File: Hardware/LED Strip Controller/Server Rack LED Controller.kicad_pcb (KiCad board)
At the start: 2 copper layers, 26 parts, among them Q1 IRF540N, Q10 IRF540N, Q11 IRF540N, Q12 IRF540N, Q13 IRF540N, Q2 IRF540N, Q3 Q_PMOS_SDG, Q4 IRF540N, Q5 IRF540N, Q6 IRF540N, Q7 IRF540N, Q8 IRF540N, Q9 IRF540N, U1 STM32F103C8Tx, U2 LM2596S-5, U3 LD1117S50TR_SOT223

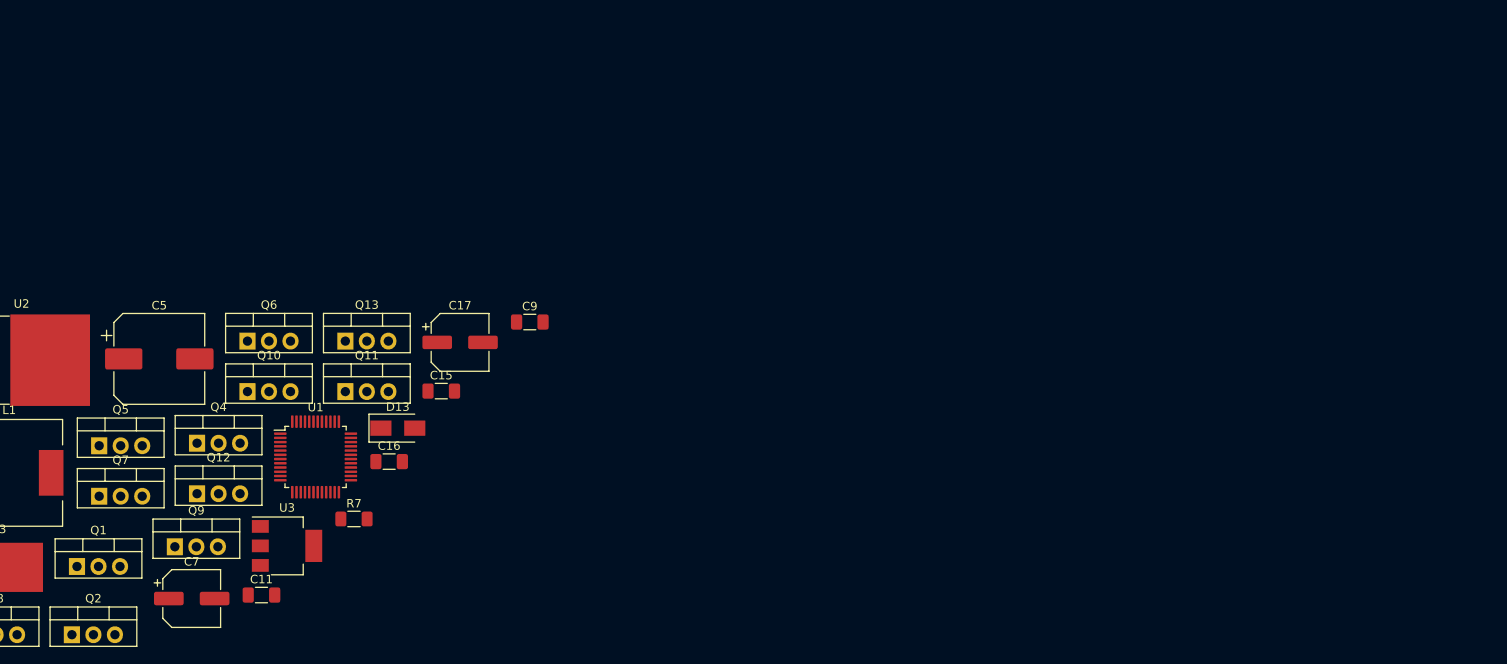
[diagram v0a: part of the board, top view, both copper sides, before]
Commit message: Adding updated PCB Schematic, still to add USB C connector and JLCPCB Part Numbers and values
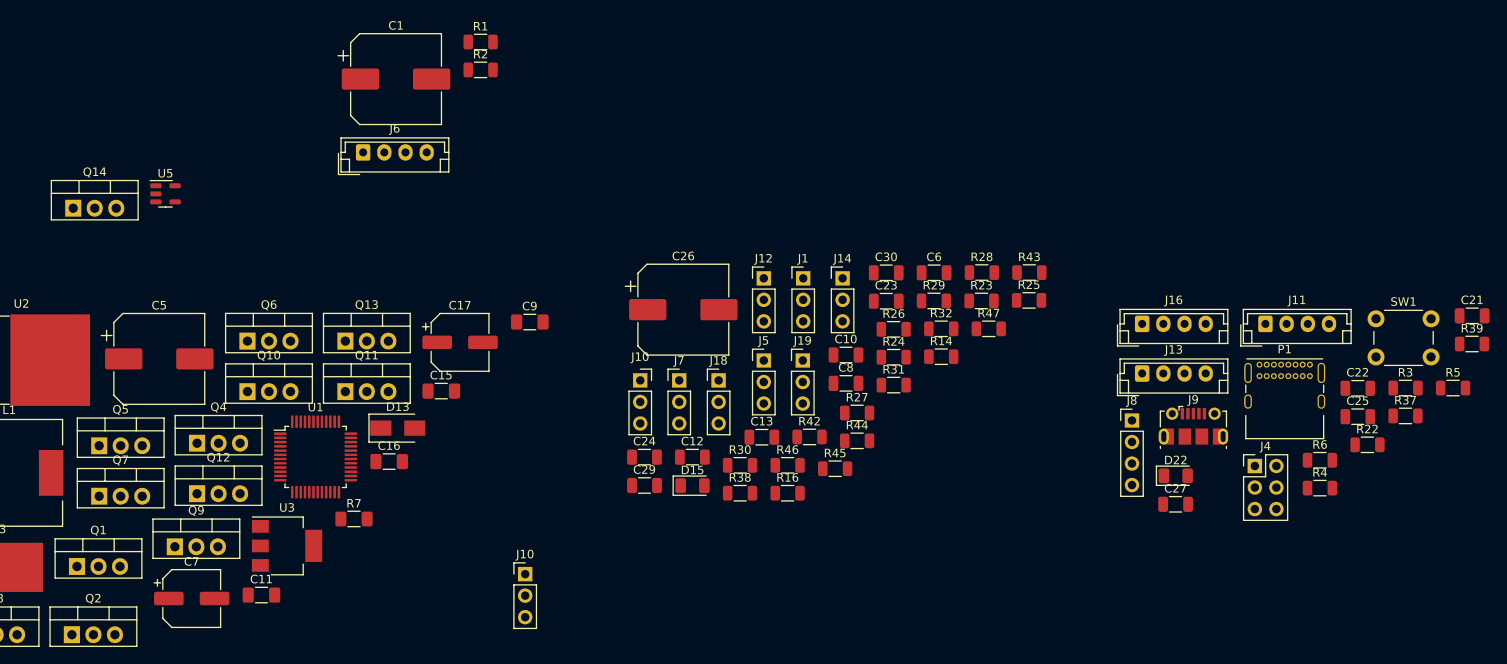
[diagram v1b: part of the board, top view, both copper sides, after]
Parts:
- added C1: C_Polarized, Capacitor_SMD:CP_Elec_10x10.5, F.Cu at (127.0, 27.9)
- added C10: 100nF, Capacitor_SMD:C_1206_3216Metric, F.Cu at (180.1, 60.5)
- added C12: 100nF, Capacitor_SMD:C_1206_3216Metric, F.Cu at (162.0, 72.5)
- added C13: 100nF, Capacitor_SMD:C_1206_3216Metric, F.Cu at (170.2, 70.2)
- added C21: 1uF, Capacitor_SMD:C_1206_3216Metric, F.Cu at (254.0, 55.9)
- added C22: 100nF, Capacitor_SMD:C_1206_3216Metric, F.Cu at (240.5, 64.4)
- added C23: 100nF, Capacitor_SMD:C_1206_3216Metric, F.Cu at (184.8, 54.1)
- added C24: 10nF, Capacitor_SMD:C_1206_3216Metric, F.Cu at (156.3, 72.5)
- added C25: 1uF, Capacitor_SMD:C_1206_3216Metric, F.Cu at (240.5, 67.8)
- added C26: C_Polarized, Capacitor_SMD:CP_Elec_10x10.5, F.Cu at (160.9, 55.1)
- added C27: 100nF, Capacitor_SMD:C_1206_3216Metric, F.Cu at (219.0, 78.1)
- added C29: 01.uF, Capacitor_SMD:C_1206_3216Metric, F.Cu at (156.3, 75.9)
- added C30: 1uF, Capacitor_SMD:C_1206_3216Metric, F.Cu at (184.8, 50.8)
- added C6: 100nF, Capacitor_SMD:C_1206_3216Metric, F.Cu at (190.5, 50.8)
- added C8: 100nF, Capacitor_SMD:C_1206_3216Metric, F.Cu at (180.1, 63.9)
- added D15: LED, LED_SMD:LED_1206_3216Metric, F.Cu at (162.0, 75.9)
- added D22: LED, LED_SMD:LED_1206_3216Metric, F.Cu at (219.0, 74.8)
- added J1: Conn_01x03_Male, Connector_PinHeader_2.54mm:PinHeader_1x03_P2.54mm_Vertical, F.Cu at (175.1, 51.5)
- added J10: Conn_01x03_Female, Connector_PinSocket_2.54mm:PinSocket_1x03_P2.54mm_Vertical, F.Cu at (155.8, 63.5)
- added J10: UART, Connector_PinHeader_2.54mm:PinHeader_1x03_P2.54mm_Vertical, F.Cu at (142.2, 86.4)
- added J11: CONN_2, Connector_JST:JST_EH_B4B-EH-A_1x04_P2.50mm_Vertical, F.Cu at (229.6, 56.8)
- added J12: Conn_01x03_Male, Connector_PinHeader_2.54mm:PinHeader_1x03_P2.54mm_Vertical, F.Cu at (170.4, 51.5)
- added J13: CONN_3, Connector_JST:JST_EH_B4B-EH-A_1x04_P2.50mm_Vertical, F.Cu at (215.1, 62.7)
- added J14: Conn_01x03_Male, Connector_PinHeader_2.54mm:PinHeader_1x03_P2.54mm_Vertical, F.Cu at (179.7, 51.5)
- added J16: CONN_4, Connector_JST:JST_EH_B4B-EH-A_1x04_P2.50mm_Vertical, F.Cu at (215.1, 56.8)
- added J18: Conn_01x03_Male, Connector_PinHeader_2.54mm:PinHeader_1x03_P2.54mm_Vertical, F.Cu at (165.1, 63.5)
- added J19: Conn_01x03_Male, Connector_PinHeader_2.54mm:PinHeader_1x03_P2.54mm_Vertical, F.Cu at (175.0, 61.1)
- added J4: Conn_02x03_Odd_Even, Connector_PinHeader_2.54mm:PinHeader_2x03_P2.54mm_Vertical, F.Cu at (228.3, 73.6)
- added J5: Conn_01x03_Female, Connector_PinHeader_2.54mm:PinHeader_1x03_P2.54mm_Vertical, F.Cu at (170.4, 61.1)
- added J6: CONN_1, Connector_JST:JST_EH_B4B-EH-A_1x04_P2.50mm_Vertical, F.Cu at (123.1, 36.6)
- added J7: Conn_01x03_Male, Connector_PinHeader_2.54mm:PinHeader_1x03_P2.54mm_Vertical, F.Cu at (160.4, 63.5)
- added J8: SWD, Connector_PinHeader_2.54mm:PinHeader_1x04_P2.54mm_Vertical, F.Cu at (213.8, 68.2)
- added J9: USB_B_Micro, Connector_USB:USB_Micro-B_Molex-105017-0001, F.Cu at (221.1, 68.9)
- added P1: USB_C_Plug, Connector_USB:USB_C_Receptacle_GCT_USB4085, F.Cu at (228.9, 61.6)
- added Q14: IRF540N, Package_TO_SOT_THT:TO-220-3_Vertical, F.Cu at (88.9, 43.2)
- added R1: 10k, Resistor_SMD:R_1206_3216Metric, F.Cu at (137.0, 23.6)
- added R14: 10K, Resistor_SMD:R_1206_3216Metric, F.Cu at (191.3, 60.7)
- added R16: R, Resistor_SMD:R_1206_3216Metric, F.Cu at (173.2, 76.8)
- added R2: 100k, Resistor_SMD:R_1206_3216Metric, F.Cu at (137.0, 26.9)
- added R22: R, Resistor_SMD:R_1206_3216Metric, F.Cu at (241.6, 71.1)
- added R23: R, Resistor_SMD:R_1206_3216Metric, F.Cu at (196.1, 54.1)
- added R24: R, Resistor_SMD:R_1206_3216Metric, F.Cu at (185.7, 60.8)
- added R25: R, Resistor_SMD:R_1206_3216Metric, F.Cu at (201.7, 54.1)
- added R26: R, Resistor_SMD:R_1206_3216Metric, F.Cu at (185.7, 57.5)
- added R27: R, Resistor_SMD:R_1206_3216Metric, F.Cu at (181.4, 67.3)
- added R28: R, Resistor_SMD:R_1206_3216Metric, F.Cu at (196.1, 50.8)
- added R29: 10K, Resistor_SMD:R_1206_3216Metric, F.Cu at (190.5, 54.1)
- added R3: R, Resistor_SMD:R_1206_3216Metric, F.Cu at (246.1, 64.4)
- added R30: 10K, Resistor_SMD:R_1206_3216Metric, F.Cu at (167.6, 73.5)
- added R31: 10K, Resistor_SMD:R_1206_3216Metric, F.Cu at (185.7, 64.0)
- added R32: 10K, Resistor_SMD:R_1206_3216Metric, F.Cu at (191.3, 57.4)
- added R37: 100K, Resistor_SMD:R_1206_3216Metric, F.Cu at (246.1, 67.7)
- added R38: R, Resistor_SMD:R_1206_3216Metric, F.Cu at (167.6, 76.8)
- added R39: 100K, Resistor_SMD:R_1206_3216Metric, F.Cu at (254.0, 59.2)
- added R4: R, Resistor_SMD:R_1206_3216Metric, F.Cu at (236.0, 76.2)
- added R42: 20R, Resistor_SMD:R_1206_3216Metric, F.Cu at (175.8, 70.2)
- added R43: 20R, Resistor_SMD:R_1206_3216Metric, F.Cu at (201.7, 50.8)
- added R44: 4.7K, Resistor_SMD:R_1206_3216Metric, F.Cu at (181.4, 70.6)
- added R45: 1M, Resistor_SMD:R_1206_3216Metric, F.Cu at (178.8, 73.9)
- added R46: 20R, Resistor_SMD:R_1206_3216Metric, F.Cu at (173.2, 73.5)
- added R47: 20R, Resistor_SMD:R_1206_3216Metric, F.Cu at (196.9, 57.4)
- added R5: R, Resistor_SMD:R_1206_3216Metric, F.Cu at (251.7, 64.4)
- added R6: R, Resistor_SMD:R_1206_3216Metric, F.Cu at (236.0, 72.9)
- added SW1: SW_Push_Dual, Button_Switch_THT:SW_PUSH_6mm, F.Cu at (242.7, 56.2)
- added U5: INA169, Package_TO_SOT_SMD:SOT-23-5, F.Cu at (99.8, 41.5)
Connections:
- C11 pad 2: GND -> CURR_SENSE
- C15 pad 2: GND -> CURR_SENSE
- C16 pad 2: GND -> CURR_SENSE
- C17 pad 2: GND -> CURR_SENSE
- C5 pad 2: GND -> CURR_SENSE
- C7 pad 2: GND -> CURR_SENSE
- C9 pad 2: GND -> CURR_SENSE
- D13 pad 2: GND -> CURR_SENSE
- Q1 pad 3: GND -> CURR_SENSE
- Q10 pad 3: GND -> CURR_SENSE
- Q11 pad 3: GND -> CURR_SENSE
- Q12 pad 3: GND -> CURR_SENSE
- Q13 pad 3: GND -> CURR_SENSE
- Q2 pad 3: GND -> CURR_SENSE
- Q4 pad 3: GND -> CURR_SENSE
- Q5 pad 3: GND -> CURR_SENSE
- Q6 pad 3: GND -> CURR_SENSE
- Q7 pad 3: GND -> CURR_SENSE
- Q8 pad 3: GND -> CURR_SENSE
- Q9 pad 3: GND -> CURR_SENSE
- R7 pad 2: GND -> CURR_SENSE
- U1 pad 10: PWM_4_GREEN -> PWM_1_GREEN
- U1 pad 11: PWM_2_BLUE -> PWM_1_RED
- U1 pad 12: PWM_2_RED -> PWM_1_BLUE
- U1 pad 13: PWM_2_GREEN -> PWM_4_GREEN
- U1 pad 14: unconnected-(U1-Pad14) -> CURR_SENSE
- U1 pad 15: unconnected-(U1-Pad15) -> VS_SENSE
- U1 pad 16: PWM_4_RED -> PWM_2_GREEN
- U1 pad 17: PWM_1_BLUE -> PWM_2_BLUE
- U1 pad 18: PWM_1_RED -> PWM_2_BLUE
- U1 pad 19: PWM_1_GREEN -> PWM_4_RED
- U1 pad 23: unconnected-(U1-Pad23) -> CURR_SENSE
- U1 pad 24: unconnected-(U1-Pad24) -> VDDA
- U1 pad 3: Net-(C2-Pad1) -> OSC32_IN
- U1 pad 32: Net-(J9-Pad2) -> STM32_USB-
- U1 pad 33: Net-(J9-Pad3) -> STM32_USB+
- U1 pad 35: unconnected-(U1-Pad35) -> CURR_SENSE
- U1 pad 36: unconnected-(U1-Pad36) -> VDDA
- U1 pad 38: unconnected-(U1-Pad38) -> FAN_SIG
- U1 pad 4: Net-(C3-Pad1) -> OSC32_OUT
- U1 pad 47: unconnected-(U1-Pad47) -> CURR_SENSE
- U1 pad 48: unconnected-(U1-Pad48) -> VDDA
- U1 pad 5: unconnected-(U1-Pad5) -> OSC_IN
- U1 pad 6: unconnected-(U1-Pad6) -> OSC_OUT
- U1 pad 7: unconnected-(U1-Pad7) -> RESET
- U1 pad 8: unconnected-(U1-Pad8) -> CURR_SENSE
- U1 pad 9: unconnected-(U1-Pad9) -> VDDA
- U2 pad 3: GND -> CURR_SENSE
- U2 pad 5: GND -> CURR_SENSE
- U3 pad 1: GND -> CURR_SENSE

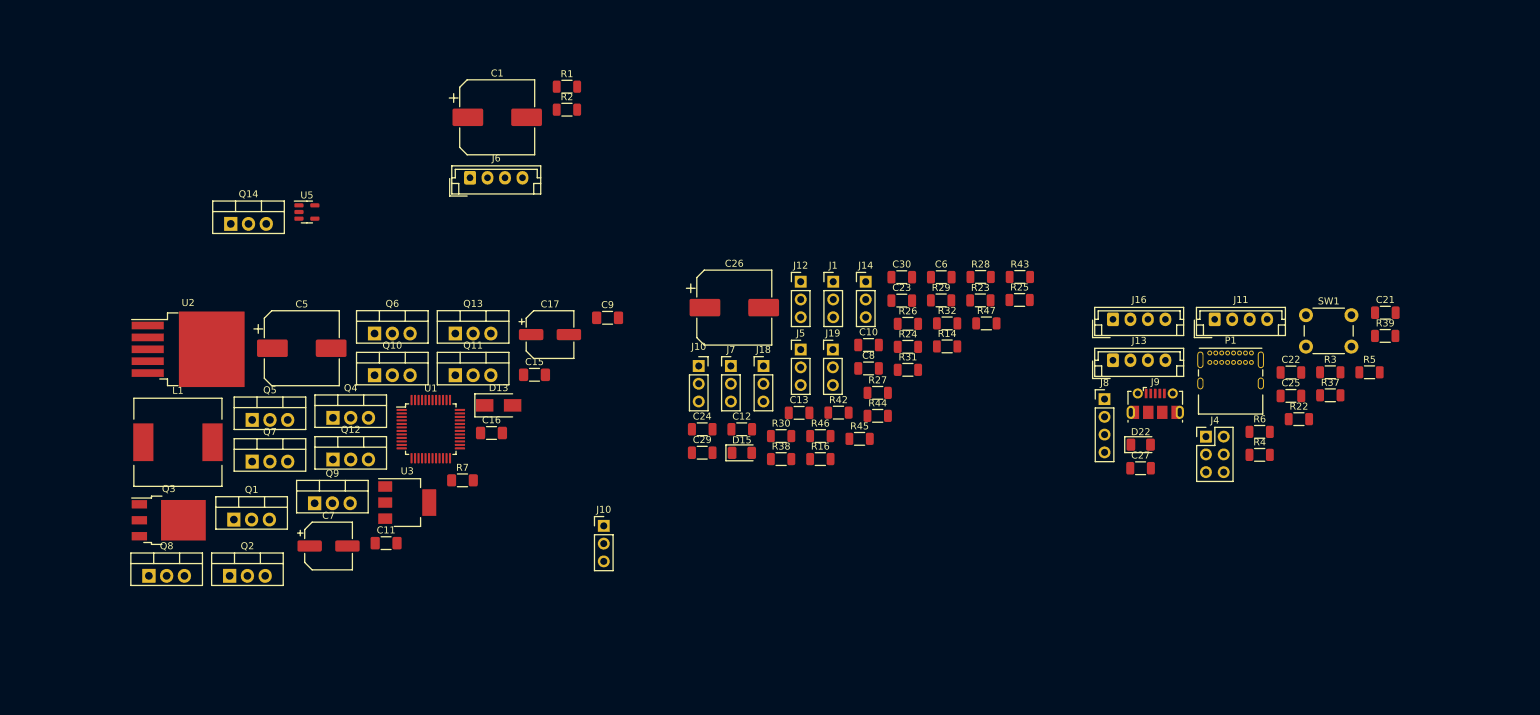
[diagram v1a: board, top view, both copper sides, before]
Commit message: Adding updated PCB Schematic, need to source JLCPCB SMT Parts and do layout
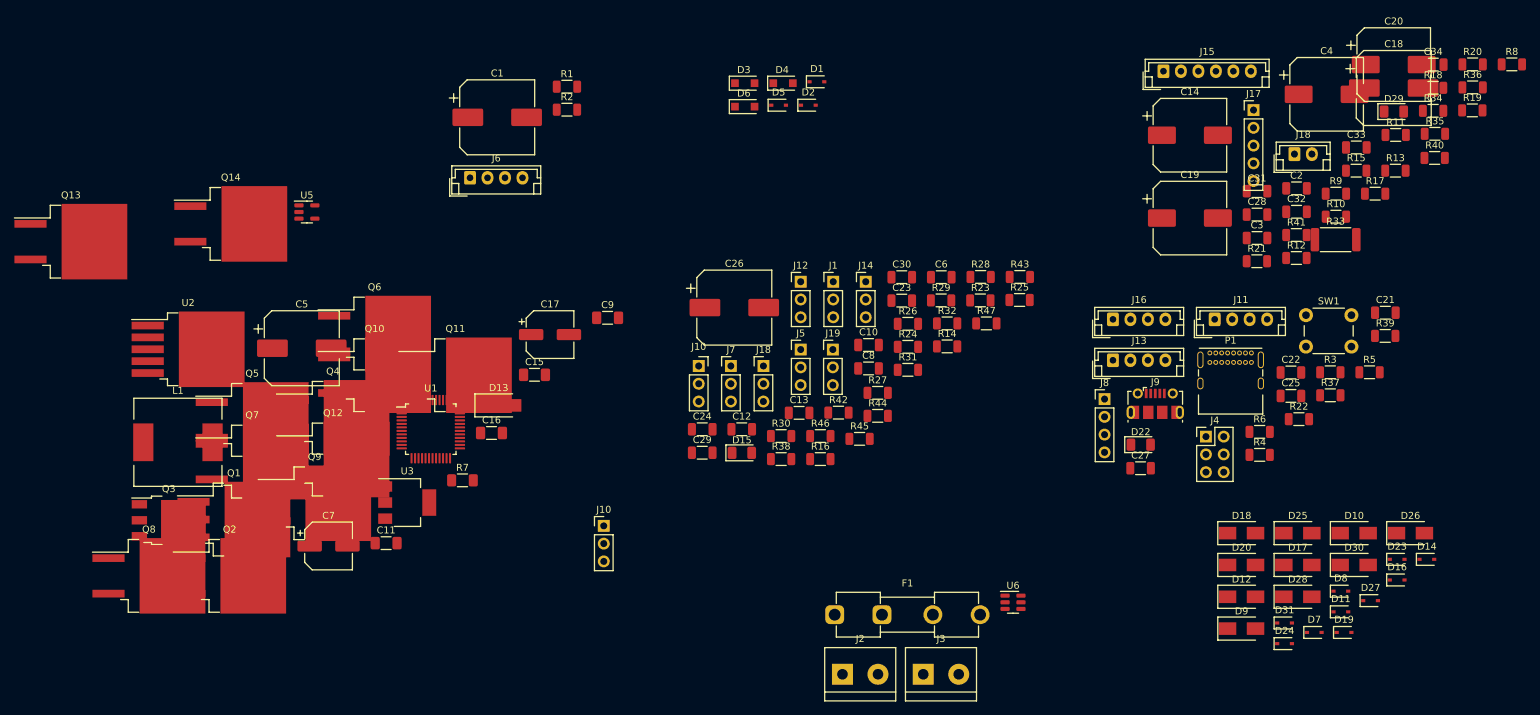
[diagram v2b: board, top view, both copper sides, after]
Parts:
- added C14: 100uF, Capacitor_SMD:CP_Elec_10x10, F.Cu at (226.1, 30.5)
- added C18: 10uF, Capacitor_SMD:CP_Elec_10x10.5, F.Cu at (255.2, 23.8)
- added C19: 100uF, Capacitor_SMD:CP_Elec_10x10, F.Cu at (226.1, 42.4)
- added C2: C, Capacitor_SMD:C_1206_3216Metric, F.Cu at (241.3, 38.1)
- added C20: 10uF, Capacitor_SMD:CP_Elec_10x10, F.Cu at (255.2, 20.4)
- added C28: 01.uF, Capacitor_SMD:C_1206_3216Metric, F.Cu at (235.7, 41.9)
- added C3: C, Capacitor_SMD:C_1206_3216Metric, F.Cu at (235.7, 45.2)
- added C31: C, Capacitor_SMD:C_1206_3216Metric, F.Cu at (235.7, 38.5)
- added C32: C, Capacitor_SMD:C_1206_3216Metric, F.Cu at (241.3, 41.5)
- added C33: 1u, Capacitor_SMD:C_1206_3216Metric, F.Cu at (249.8, 32.2)
- added C34: 10n, Capacitor_SMD:C_1206_3216Metric, F.Cu at (260.9, 20.4)
- added C4: 100uF, Capacitor_SMD:CP_Elec_10x10, F.Cu at (245.6, 24.6)
- added D1: 1N4148, Diode_SMD:D_SOD-323, F.Cu at (172.7, 22.9)
- added D10: 1N4001, Diode_SMD:D_SMA, F.Cu at (249.5, 87.4)
- added D11: 1N4148, Diode_SMD:D_SOD-323, F.Cu at (247.6, 98.7)
- added D12: 1N4001, Diode_SMD:D_SMA, F.Cu at (233.4, 96.5)
- added D14: 1N4148, Diode_SMD:D_SOD-323, F.Cu at (259.9, 91.2)
- added D16: 1N4148, Diode_SMD:D_SOD-323, F.Cu at (255.7, 94.1)
- added D17: 1N4001, Diode_SMD:D_SMA, F.Cu at (241.5, 92.0)
- added D18: 1N4001, Diode_SMD:D_SMA, F.Cu at (233.4, 87.4)
- added D19: 1N4148, Diode_SMD:D_SOD-323, F.Cu at (248.1, 101.6)
- added D2: 1N4148, Diode_SMD:D_SOD-323, F.Cu at (171.5, 26.2)
- added D20: 1N4001, Diode_SMD:D_SMA, F.Cu at (233.4, 92.0)
- added D23: 1N4148, Diode_SMD:D_SOD-323, F.Cu at (255.7, 91.2)
- added D24: 1N4148, Diode_SMD:D_SOD-323, F.Cu at (239.6, 103.2)
- added D25: 1N4001, Diode_SMD:D_SMA, F.Cu at (241.5, 87.4)
- added D26: 1N4001, Diode_SMD:D_SMA, F.Cu at (257.6, 87.4)
- added D27: 1N4148, Diode_SMD:D_SOD-323, F.Cu at (251.9, 97.0)
- added D28: 1N4001, Diode_SMD:D_SMA, F.Cu at (241.5, 96.5)
- added D29: RED LED, LED_SMD:LED_1206_3216Metric, F.Cu at (255.2, 27.1)
- added D3: 1N4001, Diode_SMD:D_SOD-123F, F.Cu at (162.4, 23.1)
- added D30: 1N5001, Diode_SMD:D_SMA, F.Cu at (249.5, 92.0)
- added D31: 1N4148, Diode_SMD:D_SOD-323, F.Cu at (239.6, 100.2)
- added D4: 1N4001, Diode_SMD:D_SOD-123F, F.Cu at (167.9, 23.1)
- added D5: 1N4148, Diode_SMD:D_SOD-323, F.Cu at (167.2, 26.2)
- added D6: 1N4001, Diode_SMD:D_SOD-123F, F.Cu at (162.4, 26.4)
- added D7: 1N4148, Diode_SMD:D_SOD-323, F.Cu at (243.8, 101.6)
- added D8: 1N4148, Diode_SMD:D_SOD-323, F.Cu at (247.6, 95.7)
- added D9: 1N4001, Diode_SMD:D_SMA, F.Cu at (233.4, 101.0)
- added F1: 1A, Fuse:Fuseholder_Clip-5x20mm_Eaton_1A5601-01_Inline_P20.80x6.76mm_D1.70mm_Horizontal, F.Cu at (175.3, 99.1)
- added J15: Conn_01x06_Female, Connector_JST:JST_EH_B6B-EH-A_1x06_P2.50mm_Vertical, F.Cu at (222.3, 21.4)
- added J17: TST, Connector_PinHeader_2.54mm:PinHeader_1x05_P2.54mm_Vertical, F.Cu at (235.2, 26.9)
- added J18: Conn_01x02_Female, Connector_JST:JST_EH_B2B-EH-A_1x02_P2.50mm_Vertical, F.Cu at (241.0, 33.2)
- added J2: Screw_Terminal_01x02, TerminalBlock:TerminalBlock_bornier-2_P5.08mm, F.Cu at (176.4, 107.6)
- added J3: PWR_SWITCH, TerminalBlock:TerminalBlock_bornier-2_P5.08mm, F.Cu at (187.9, 107.6)
- added R10: 10K, Resistor_SMD:R_1206_3216Metric, F.Cu at (246.9, 42.1)
- added R11: 10K, Resistor_SMD:R_1206_3216Metric, F.Cu at (255.5, 30.5)
- added R12: 100K, Resistor_SMD:R_1206_3216Metric, F.Cu at (241.3, 48.1)
- added R13: 100K, Resistor_SMD:R_1206_3216Metric, F.Cu at (255.4, 35.6)
- added R15: 10K, Resistor_SMD:R_1206_3216Metric, F.Cu at (249.8, 35.6)
- added R17: 100K, Resistor_SMD:R_1206_3216Metric, F.Cu at (252.5, 38.9)
- added R18: 10K, Resistor_SMD:R_1206_3216Metric, F.Cu at (260.8, 23.7)
- added R19: 10K, Resistor_SMD:R_1206_3216Metric, F.Cu at (266.4, 26.9)
- added R20: 100K, Resistor_SMD:R_1206_3216Metric, F.Cu at (266.5, 20.4)
- added R21: 100K, Resistor_SMD:R_1206_3216Metric, F.Cu at (235.6, 48.5)
- added R33: 0.1R, Resistor_SMD:R_2512_6332Metric, F.Cu at (246.9, 45.4)
- added R34: 10K, Resistor_SMD:R_1206_3216Metric, F.Cu at (260.8, 27.0)
- added R35: 1M, Resistor_SMD:R_1206_3216Metric, F.Cu at (261.1, 30.3)
- added R36: 10M, Resistor_SMD:R_1206_3216Metric, F.Cu at (266.5, 23.7)
- added R40: 10K, Resistor_SMD:R_1206_3216Metric, F.Cu at (261.1, 33.8)
- added R41: 100K, Resistor_SMD:R_1206_3216Metric, F.Cu at (241.3, 44.8)
- added R8: 10K, Resistor_SMD:R_1206_3216Metric, F.Cu at (272.1, 20.4)
- added R9: 100K, Resistor_SMD:R_1206_3216Metric, F.Cu at (246.9, 38.9)
- added U6: USBLC6-2SC6, Package_TO_SOT_SMD:SOT-23-6, F.Cu at (200.8, 97.3)
- C1, C26: value C_Polarized -> 100uF
- D15: value LED -> Green LED
- D22: value LED -> Blue LED
- Q1: value IRF540N -> IRF510N; footprint Package_TO_SOT_THT:TO-220-3_Vertical -> Package_TO_SOT_SMD:TO-263-3_TabPin2
- Q10, Q11, Q12, Q13, Q14, Q2, Q4, Q5, Q6, Q7, Q8, Q9: value IRF540N -> IRF510N; footprint Package_TO_SOT_THT:TO-220-3_Vertical -> Package_TO_SOT_SMD:TO-263-2
- R16, R22, R38: value R -> 15K
- R23, R25, R26, R3, R4: value R -> 10K
- R24, R27, R28, R5, R6: value R -> 100K
- moved Q13 56.5 mm to (66.0, 45.7)
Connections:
- net SMPS_5V renamed PWR_5V
- net USB_5V renamed USB_VBUS
- C10 pad 1: VDDA -> +3V3
- C12 pad 1: VDDA -> +3V3
- C23 pad 1: VDDA -> +3V3
- C24 pad 1: VDDA -> +3V3
- C25 pad 1: VDDA -> +3V3
- C27 pad 1: VDDA -> +3V3
- C29 pad 1: VDDA -> +3V3
- C6 pad 1: VDDA -> +3V3
- C8 pad 1: VDDA -> +3V3
- J4 pad 5: VDDA -> +3V3
- J4 pad 6: VDDA -> +3V3
- J8 pad 1: VDDA -> +3V3
- J9 pad 6: CURR_SENSE -> unconnected-(J9-Pad6)
- R14 pad 1: VDDA -> +3V3
- R16 pad 1: VDDA -> +3V3
- R29 pad 1: VDDA -> +3V3
- R30 pad 1: VDDA -> +3V3
- R31 pad 1: VDDA -> +3V3
- R32 pad 1: VDDA -> +3V3
- U1 pad 24: VDDA -> +3V3
- U1 pad 32: STM32_USB- -> /STM32_USB-
- U1 pad 33: STM32_USB+ -> /STM32_USB+
- U1 pad 36: VDDA -> +3V3
- U1 pad 48: VDDA -> +3V3
- U5 pad 5: VDDA -> +3V3
